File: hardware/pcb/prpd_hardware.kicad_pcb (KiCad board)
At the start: 2 copper layers, 22 x 54.5 mm, 16 parts, among them J1 RJ45_Shielded, J11 RJ45_Shielded, J2 Conn_01x03, T1 , T2 , T3 , T4 , T5 , T6 , T7 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

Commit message: hardware: add power symbols and screenshots
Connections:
- net Net-(C1-Pad1) renamed GND
- net Net-(C1-Pad2) renamed +3V3

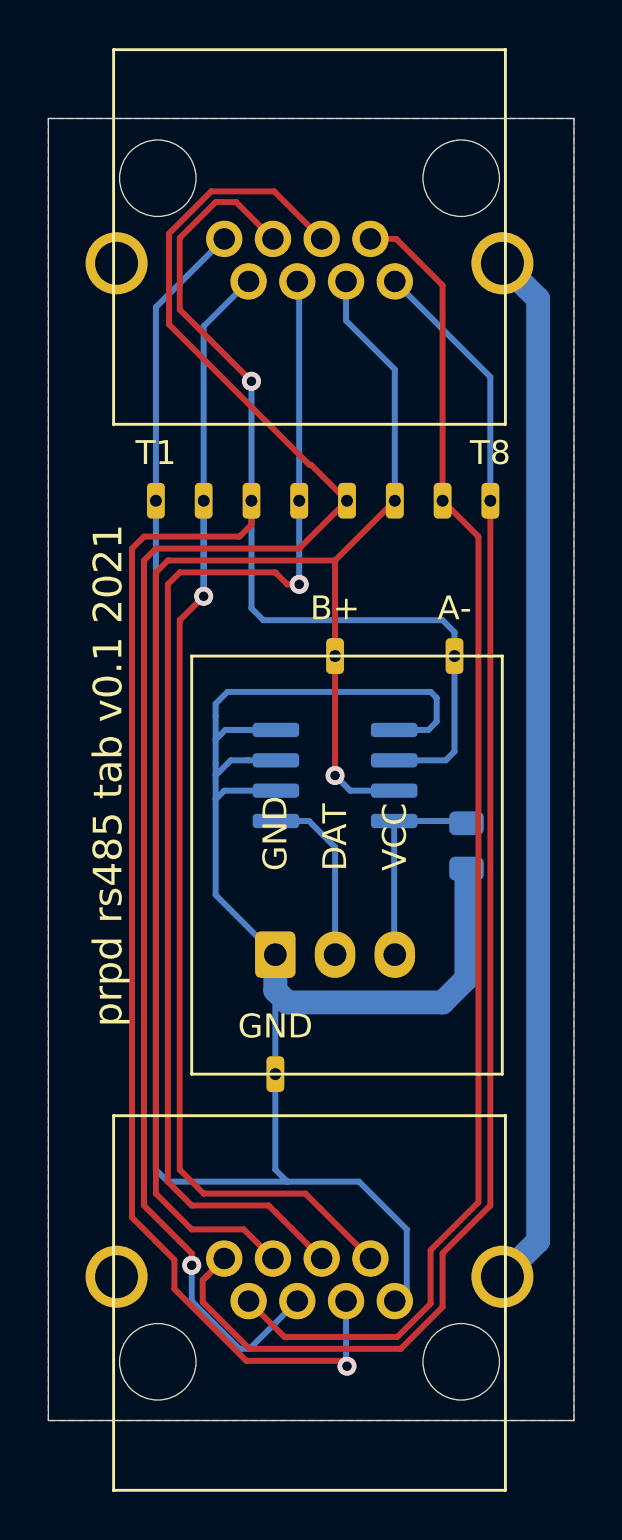
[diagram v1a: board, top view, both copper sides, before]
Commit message: fix mixup of datalines
datalines of transceivers do swap A and B. the relevant information is
+/- or non inverting/inverting. serial ttl output was inverted; readings
where broken, most symbols where around 255.
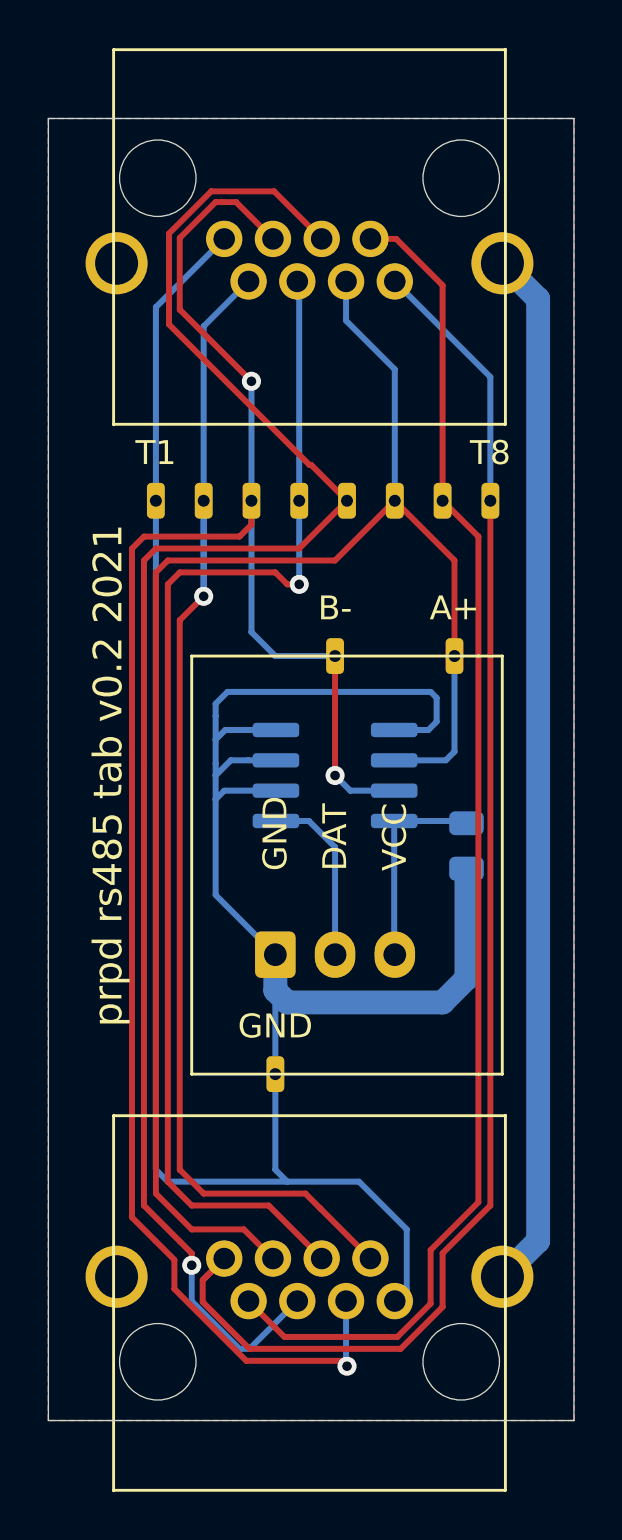
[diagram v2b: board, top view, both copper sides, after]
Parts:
- TI2: value A- -> A+
- TI3: value B+ -> B-
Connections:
- TI2 pad 1: Net-(J1-Pad3) -> Net-(J1-Pad6)
- TI3 pad 1: Net-(J1-Pad6) -> Net-(J1-Pad3)
- U1 pad 6: Net-(J1-Pad3) -> Net-(J1-Pad6)
- U1 pad 7: Net-(J1-Pad6) -> Net-(J1-Pad3)
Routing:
- net Net-(J1-Pad3): track 88.4 -> 85.0 mm, vias 2 -> 3
- net Net-(J1-Pad6): track 65.0 -> 67.0 mm, vias 1 -> 0
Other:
- board text added: "."
- board text added: "A+"
- board text added: "B-"
- board text added: "prpd rs485 tab v0.2 2021"
- board text removed: "A-"
- board text removed: "B+"
- board text removed: "prpd rs485 tab v0.1 2021"
